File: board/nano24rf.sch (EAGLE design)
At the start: 26 parts, among them CN1 1X4-CLEANBIG, CN2 1X4-CLEANBIG, CN3 1X4-CLEANBIG, CN4 1X4-CLEANBIG

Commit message: before route
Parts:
- removed C1, C2: (no value), ATTAMI-V0.00:CAP0805
- removed CN1, CN2, CN3, CN4, I2CPORT: 1X4-CLEANBIG, adafruit:1X4-CLEANBIG
- removed FET1, FET2, JP6: (no value), ATTAMI-V0.00:HEADER-1X2ROUND
- removed SJ1, SJ2: JUMPER-PAD-3-2OF3_NC_BY_TRACE_SMALL, ATTAMI-V0.00:JUMPER-PAD-3-2OF3_NC_BY_TRACE_SMALL
- removed SW1: (no value), microbuilder:SWITCH_SPST
- removed U$2: NRF24, ATTAMI-V0.00:NRF24
- removed U2: (no value), microbuilder:VREG_SOT23SOT23_WIDE
- added D3, D4: (no value), dp_devices:DIODE-DO-214AC
- added Q3, Q4: (no value), adafruit:MOSFET-NWAVE
- added R5, R6: (no value), ATTAMI-V0.00:RESISTOR0805-RES
- added U$6, U$8: 1X3SMD, nanorf24:1X3SMD
- added U$7: 1X7-SMDPADS, nanorf24:1X7-SMDPADS
- JP3: device adafruit:PINHD-1X1CB -> pinhead+:PINHD-2X3SMT
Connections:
- removed net IRQ: U$2.IRQ
- removed net N$1 (its old number): D1.A, FET1.2, Q1.D
- removed net RAW: JP3.1, JP6.1, SW1.P
- removed net RX: CN4.3, JP2.14
- removed net TX: CN4.2, JP2.15
- removed net V-ADJ: C2.1, SJ1.1, U2.VOUT
- removed net V-NRF: SJ1.2, U$2.VCC
- new net D10: JP2.3, R3.1
- new net D9: JP2.4, R4.1
- new net FET01: D1.A, Q1.D, U$8.P$1
- new net FET02: D2.A, Q2.D, U$8.P$3
- new net FET03: D3.A, Q3.D, U$6.P$1
- new net FET04: D4.A, Q4.D, U$6.P$3
- new net N$5: Q4.G, R4.2
- net 3V3: no longer R3.2, R4.2, SJ1.3, SJ2.1
- net 5V: now also JP3.2, R5.1; no longer C1.1, CN4.1, JP1.12, SJ2.3, U2.VIN
- net CE: now also JP2.6, U$7.CE; no longer JP2.3, U$2.CE
- net CSN: now also JP2.5, U$7.CSN; no longer JP2.4, U$2.CSN
- net D3: no longer R1.1
- net D6: now also R1.1
- net GND: now also JP3.6, Q3.S, Q4.S, R6.1, U$7.GND; no longer C1.2, C2.2, CN4.4, I2CPORT.4, JP6.2, U$2.GND, U2.GND
- net MISO: now also JP3.1, U$7.MISO; no longer JP2.1, U$2.MISO
- net MOSI: now also JP3.4, U$7.MOSI; no longer JP2.2, U$2.MOSI
- net N$4: now also Q3.G, R3.2; no longer D2.A, FET2.2, Q2.D
- net N$6: now also R5.2, R6.2, U$7.3V3; no longer I2CPORT.3, SJ2.2
- net RST: now also JP3.5; no longer JP2.13
- net SCK: now also JP3.3, U$7.SCK; no longer JP1.1, U$2.SCK
- net SCL: no longer I2CPORT.1, R4.1
- net SDA: no longer I2CPORT.2, R3.1
- net VIN: now also D3.C, D4.C, U$6.P$2, U$8.P$2; no longer FET1.1, FET2.1, SW1.S
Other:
- note added: "mosfets"
- note removed: "* 5V on the right rail should not be connected to nano! this location is originaly for a reset pin."
- note removed: "NRF24"
- moved on the sheet: D1, D2, Q1, Q2, R1, R2, R3, R4

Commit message: added lib, need to fix volt div placment
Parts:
- JP3: device pinhead+:PINHD-2X3SMT -> nano24rf:PINHD-2X3SMT
- U$7: device nanorf24:1X7-SMDPADS -> nano24rf:1X7-SMDPADS
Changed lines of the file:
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@@
 <part name="JP1" library="microbuilder" deviceset="HEADER-1X15" device=""/>
 <part name="JP2" library="microbuilder" deviceset="HEADER-1X15" device=""/>
-<part name="JP3" library="pinhead+" deviceset="PINHD-2X3" device="SMT"/>
-<part name="U$7" library="nanorf24" deviceset="1X7-SMDPADS" device=""/>
+<part name="JP3" library="nano24rf" deviceset="PINHD-2X3" device="SMT"/>
+<part name="U$7" library="nano24rf" deviceset="1X7-SMDPADS" device=""/>
 <part name="Q2" library="adafruit" deviceset="MOSFET-N" device="WAVE"/>
 <part name="D2" library="dp_devices" deviceset="DIODE" device="-DO-214AC"/>

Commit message: ready to grb
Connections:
- removed net N$1: Q2.G, R2.2
- removed net N$2: Q1.G, R1.2
- removed net N$4: Q3.G, R3.2
- removed net N$5: Q4.G, R4.2
- net 5V: now also R1.1; no longer R5.1
- net D10: now also Q3.G, R5.2; no longer R3.1
- net D5: now also Q2.G, R4.2; no longer R2.1
- net D6: now also Q1.G, R3.2; no longer R1.1
- net D9: now also Q4.G, R6.2; no longer R4.1
- net GND: now also R2.1, R3.1, R4.1, R5.1
- net N$6: now also R1.2, R2.2; no longer R5.2, R6.2
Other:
- moved on the sheet: R1, R2, R3, R4, R5, R6
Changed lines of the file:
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@@
 <part name="D1" library="dp_devices" deviceset="DIODE" device="-DO-214AC"/>
 <part name="U$3" library="ATTAMI-V0.00" deviceset="GND" device=""/>
-<part name="R1" library="ATTAMI-V0.00" deviceset="RESISTOR" device="0805-RES"/>
 <part name="U$5" library="ATTAMI-V0.00" deviceset="GND" device=""/>
 <part name="JP1" library="microbuilder" deviceset="HEADER-1X15" device=""/>
@@
 <part name="D2" library="dp_devices" deviceset="DIODE" device="-DO-214AC"/>
 <part name="U$1" library="ATTAMI-V0.00" deviceset="GND" device=""/>
-<part name="R2" library="ATTAMI-V0.00" deviceset="RESISTOR" device="0805-RES"/>
 <part name="Q3" library="adafruit" deviceset="MOSFET-N" device="WAVE"/>
 <part name="D3" library="dp_devices" deviceset="DIODE" device="-DO-214AC"/>
 <part name="U$2" library="ATTAMI-V0.00" deviceset="GND" device=""/>
-<part name="R3" library="ATTAMI-V0.00" deviceset="RESISTOR" device="0805-RES"/>
 <part name="Q4" library="adafruit" deviceset="MOSFET-N" device="WAVE"/>
 <part name="D4" library="dp_devices" deviceset="DIODE" device="-DO-214AC"/>
 <part name="U$4" library="ATTAMI-V0.00" deviceset="GND" device=""/>
-<part name="R4" library="ATTAMI-V0.00" deviceset="RESISTOR" device="0805-RES"/>
 <part name="U$6" library="nanorf24" deviceset="1X3SMD" device=""/>
 <part name="U$8" library="nanorf24" deviceset="1X3SMD" device=""/>
+<part name="R1" library="ATTAMI-V0.00" deviceset="RESISTOR" device="0805-RES"/>
+<part name="R2" library="ATTAMI-V0.00" deviceset="RESISTOR" device="0805-RES"/>
+<part name="R4" library="ATTAMI-V0.00" deviceset="RESISTOR" device="0805-RES"/>
+<part name="R3" library="ATTAMI-V0.00" deviceset="RESISTOR" device="0805-RES"/>
+<part name="R6" library="ATTAMI-V0.00" deviceset="RESISTOR" device="0805-RES"/>
 <part name="R5" library="ATTAMI-V0.00" deviceset="RESISTOR" device="0805-RES"/>
-<part name="R6" library="ATTAMI-V0.00" deviceset="RESISTOR" device="0805-RES"/>
 </parts>
 <sheets>
@@
 <instance part="D1" gate="D" x="35.56" y="104.14" rot="R180"/>
 <instance part="U$3" gate="1" x="38.1" y="86.36"/>
-<instance part="R1" gate="G$1" x="25.4" y="93.98"/>
 <instance part="U$5" gate="1" x="27.94" y="27.94"/>
 <instance part="JP1" gate="G$1" x="45.72" y="48.26"/>
@@
 <instance part="D2" gate="D" x="35.56" y="132.08" rot="R180"/>
 <instance part="U$1" gate="1" x="38.1" y="114.3"/>
-<instance part="R2" gate="G$1" x="25.4" y="121.92"/>
 <instance part="Q3" gate="G$1" x="106.68" y="93.98"/>
 <instance part="D3" gate="D" x="106.68" y="101.6" rot="R180"/>
 <instance part="U$2" gate="1" x="109.22" y="83.82"/>
-<instance part="R3" gate="G$1" x="96.52" y="91.44"/>
 <instance part="Q4" gate="G$1" x="106.68" y="121.92"/>
 <instance part="D4" gate="D" x="106.68" y="129.54" rot="R180"/>
 <instance part="U$4" gate="1" x="109.22" y="111.76"/>
-<instance part="R4" gate="G$1" x="96.52" y="119.38"/>
 <instance part="U$6" gate="G$1" x="147.32" y="104.14" rot="R90"/>
 <instance part="U$8" gate="G$1" x="76.2" y="106.68" rot="R90"/>
-<instance part="R5" gate="G$1" x="73.66" y="15.24"/>
-<instance part="R6" gate="G$1" x="73.66" y="10.16"/>
+<instance part="R1" gate="G$1" x="73.66" y="15.24"/>
+<instance part="R2" gate="G$1" x="73.66" y="10.16"/>
+<instance part="R4" gate="G$1" x="30.48" y="116.84" rot="R90"/>
+<instance part="R3" gate="G$1" x="30.48" y="88.9" rot="R90"/>
+<instance part="R6" gate="G$1" x="101.6" y="114.3" rot="R90"/>
+<instance part="R5" gate="G$1" x="101.6" y="86.36" rot="R90"/>
 </instances>
 <busses>
@@
 <pinref part="U$3" gate="1" pin="GND"/>
 <wire x1="38.1" y1="88.9" x2="38.1" y2="91.44" width="0.1524" layer="91"/>
+<pinref part="R3" gate="G$1" pin="1"/>
+<wire x1="30.48" y1="83.82" x2="33.02" y2="83.82" width="0.1524" layer="91"/>
+<wire x1="33.02" y1="83.82" x2="33.02" y2="88.9" width="0.1524" layer="91"/>
+<wire x1="33.02" y1="88.9" x2="38.1" y2="88.9" width="0.1524" layer="91"/>
+<junction x="38.1" y="88.9"/>
 </segment>
 <segment>
@@
 <wire x1="58.42" y1="10.16" x2="68.58" y2="10.16" width="0.1524" layer="91"/>
 <label x="63.5" y="10.16" size="1.778" layer="95"/>
-<pinref part="R6" gate="G$1" pin="1"/>
+<pinref part="R2" gate="G$1" pin="1"/>
 </segment>
 <segment>
@@
 <pinref part="U$1" gate="1" pin="GND"/>
 <wire x1="38.1" y1="116.84" x2="38.1" y2="119.38" width="0.1524" layer="91"/>
+<pinref part="R4" gate="G$1" pin="1"/>
+<wire x1="30.48" y1="111.76" x2="33.02" y2="111.76" width="0.1524" layer="91"/>
+<wire x1="33.02" y1="111.76" x2="33.02" y2="116.84" width="0.1524" layer="91"/>
+<wire x1="33.02" y1="116.84" x2="38.1" y2="116.84" width="0.1524" layer="91"/>
+<junction x="38.1" y="116.84"/>
 </segment>
 <segment>
@@
 <pinref part="U$2" gate="1" pin="GND"/>
 <wire x1="109.22" y1="86.36" x2="109.22" y2="88.9" width="0.1524" layer="91"/>
+<pinref part="R5" gate="G$1" pin="1"/>
+<wire x1="101.6" y1="81.28" x2="104.14" y2="81.28" width="0.1524" layer="91"/>
+<wire x1="104.14" y1="81.28" x2="104.14" y2="86.36" width="0.1524" layer="91"/>
+<wire x1="104.14" y1="86.36" x2="109.22" y2="86.36" width="0.1524" layer="91"/>
+<junction x="109.22" y="86.36"/>
 </segment>
 <segment>
@@
 <pinref part="U$4" gate="1" pin="GND"/>
 <wire x1="109.22" y1="114.3" x2="109.22" y2="116.84" width="0.1524" layer="91"/>
+<pinref part="R6" gate="G$1" pin="1"/>
+<wire x1="101.6" y1="109.22" x2="104.14" y2="109.22" width="0.1524" layer="91"/>
+<wire x1="104.14" y1="109.22" x2="104.14" y2="114.3" width="0.1524" layer="91"/>
+<wire x1="104.14" y1="114.3" x2="109.22" y2="114.3" width="0.1524" layer="91"/>
+<junction x="109.22" y="114.3"/>
 </segment>
 </net>
@@
 </segment>
 </net>
-<net name="N$2" class="0">
-<segment>
-<pinref part="Q1" gate="G$1" pin="G"/>
-<pinref part="R1" gate="G$1" pin="2"/>
-<wire x1="30.48" y1="93.98" x2="33.02" y2="93.98" width="0.1524" layer="91"/>
-</segment>
-</net>
 <net name="D5" class="0">
 <segment>
@@
 </segment>
 <segment>
-<pinref part="R2" gate="G$1" pin="1"/>
-<wire x1="20.32" y1="121.92" x2="12.7" y2="121.92" width="0.1524" layer="91"/>
 <label x="15.24" y="121.92" size="1.778" layer="95"/>
+<pinref part="Q2" gate="G$1" pin="G"/>
+<wire x1="30.48" y1="121.92" x2="33.02" y2="121.92" width="0.1524" layer="91"/>
+<pinref part="R4" gate="G$1" pin="2"/>
+<wire x1="12.7" y1="121.92" x2="30.48" y2="121.92" width="0.1524" layer="91"/>
+<junction x="30.48" y="121.92"/>
 </segment>
 </net>
@@
 </segment>
 <segment>
-<pinref part="R1" gate="G$1" pin="1"/>
-<wire x1="20.32" y1="93.98" x2="12.7" y2="93.98" width="0.1524" layer="91"/>
 <label x="15.24" y="93.98" size="1.778" layer="95"/>
+<pinref part="Q1" gate="G$1" pin="G"/>
+<wire x1="30.48" y1="93.98" x2="33.02" y2="93.98" width="0.1524" layer="91"/>
+<pinref part="R3" gate="G$1" pin="2"/>
+<wire x1="12.7" y1="93.98" x2="30.48" y2="93.98" width="0.1524" layer="91"/>
+<junction x="30.48" y="93.98"/>
 </segment>
 </net>
@@
 <wire x1="58.42" y1="15.24" x2="68.58" y2="15.24" width="0.1524" layer="91"/>
 <label x="63.5" y="15.24" size="1.778" layer="95"/>
-<pinref part="R5" gate="G$1" pin="1"/>
+<pinref part="R1" gate="G$1" pin="1"/>
 </segment>
 </net>
@@
 </segment>
 <segment>
-<pinref part="R3" gate="G$1" pin="1"/>
-<wire x1="91.44" y1="91.44" x2="83.82" y2="91.44" width="0.1524" layer="91"/>
 <label x="86.36" y="91.44" size="1.778" layer="95"/>
+<pinref part="Q3" gate="G$1" pin="G"/>
+<wire x1="101.6" y1="91.44" x2="104.14" y2="91.44" width="0.1524" layer="91"/>
+<pinref part="R5" gate="G$1" pin="2"/>
+<wire x1="83.82" y1="91.44" x2="101.6" y2="91.44" width="0.1524" layer="91"/>
+<junction x="101.6" y="91.44"/>
 </segment>
 </net>
@@
 </segment>
 <segment>
-<pinref part="R4" gate="G$1" pin="1"/>
-<wire x1="91.44" y1="119.38" x2="83.82" y2="119.38" width="0.1524" layer="91"/>
 <label x="86.36" y="119.38" size="1.778" layer="95"/>
+<pinref part="Q4" gate="G$1" pin="G"/>
+<wire x1="101.6" y1="119.38" x2="104.14" y2="119.38" width="0.1524" layer="91"/>
+<pinref part="R6" gate="G$1" pin="2"/>
+<wire x1="101.6" y1="119.38" x2="83.82" y2="119.38" width="0.1524" layer="91"/>
+<junction x="101.6" y="119.38"/>
 </segment>
 </net>
@@
 </segment>
 </net>
-<net name="N$1" class="0">
-<segment>
-<pinref part="Q2" gate="G$1" pin="G"/>
-<pinref part="R2" gate="G$1" pin="2"/>
-<wire x1="30.48" y1="121.92" x2="33.02" y2="121.92" width="0.1524" layer="91"/>
-</segment>
-</net>
 <net name="FET03" class="0">
 <segment>
@@
 </segment>
 </net>
-<net name="N$4" class="0">
-<segment>
-<pinref part="Q3" gate="G$1" pin="G"/>
-<pinref part="R3" gate="G$1" pin="2"/>
-<wire x1="101.6" y1="91.44" x2="104.14" y2="91.44" width="0.1524" layer="91"/>
-</segment>
-</net>
 <net name="FET04" class="0">
 <segment>
@@
 </segment>
 </net>
-<net name="N$5" class="0">
-<segment>
-<pinref part="Q4" gate="G$1" pin="G"/>
-<pinref part="R4" gate="G$1" pin="2"/>
-<wire x1="101.6" y1="119.38" x2="104.14" y2="119.38" width="0.1524" layer="91"/>
-</segment>
-</net>
 <net name="N$6" class="0">
 <segment>
 <wire x1="81.28" y1="2.54" x2="81.28" y2="10.16" width="0.1524" layer="91"/>
-<pinref part="R5" gate="G$1" pin="2"/>
+<pinref part="R1" gate="G$1" pin="2"/>
 <wire x1="81.28" y1="10.16" x2="81.28" y2="15.24" width="0.1524" layer="91"/>
 <wire x1="81.28" y1="15.24" x2="78.74" y2="15.24" width="0.1524" layer="91"/>
 <pinref part="U$7" gate="G$1" pin="3V3"/>
-<pinref part="R6" gate="G$1" pin="2"/>
+<pinref part="R2" gate="G$1" pin="2"/>
 <wire x1="78.74" y1="10.16" x2="81.28" y2="10.16" width="0.1524" layer="91"/>
 <junction x="81.28" y="10.16"/>

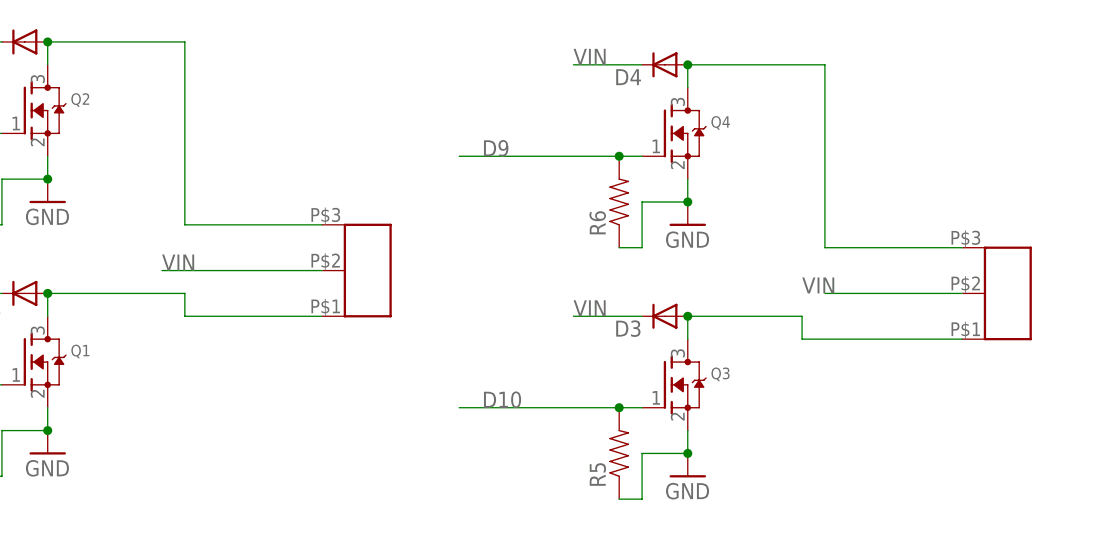
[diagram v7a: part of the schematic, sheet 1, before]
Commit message: added FATPAD4
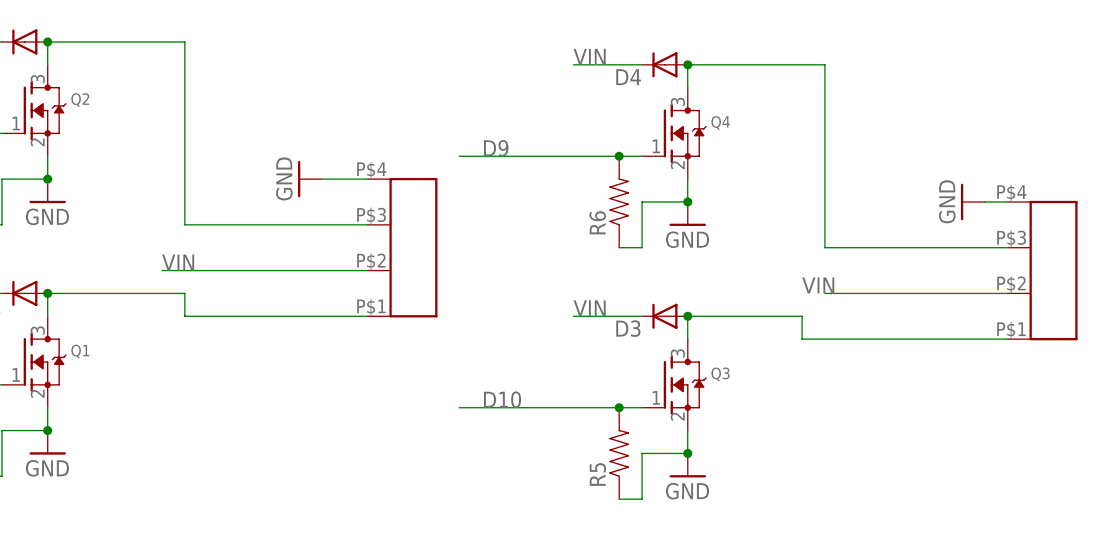
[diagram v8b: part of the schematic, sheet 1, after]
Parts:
- U$6, U$8: value 1X3SMD -> FATPAD4; device nanorf24:1X3SMD -> nano24rf:FATPAD4
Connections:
- net GND: now also U$6.P$4, U$8.P$4
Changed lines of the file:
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@@
 <part name="D4" library="dp_devices" deviceset="DIODE" device="-DO-214AC"/>
 <part name="U$4" library="ATTAMI-V0.00" deviceset="GND" device=""/>
-<part name="U$6" library="nanorf24" deviceset="1X3SMD" device=""/>
-<part name="U$8" library="nanorf24" deviceset="1X3SMD" device=""/>
+<part name="U$6" library="nano24rf" deviceset="FATPAD4" device=""/>
+<part name="U$8" library="nano24rf" deviceset="FATPAD4" device=""/>
 <part name="R1" library="ATTAMI-V0.00" deviceset="RESISTOR" device="0805-RES"/>
 <part name="R2" library="ATTAMI-V0.00" deviceset="RESISTOR" device="0805-RES"/>
@@
 <part name="R6" library="ATTAMI-V0.00" deviceset="RESISTOR" device="0805-RES"/>
 <part name="R5" library="ATTAMI-V0.00" deviceset="RESISTOR" device="0805-RES"/>
+<part name="U$9" library="ATTAMI-V0.00" deviceset="GND" device=""/>
+<part name="U$10" library="ATTAMI-V0.00" deviceset="GND" device=""/>
 </parts>
 <sheets>
@@
 <instance part="R6" gate="G$1" x="101.6" y="114.3" rot="R90"/>
 <instance part="R5" gate="G$1" x="101.6" y="86.36" rot="R90"/>
+<instance part="U$9" gate="1" x="139.7" y="114.3" rot="R270"/>
+<instance part="U$10" gate="1" x="66.04" y="116.84" rot="R270"/>
 </instances>
 <busses>
@@
 <junction x="109.22" y="114.3"/>
 </segment>
+<segment>
+<pinref part="U$10" gate="1" pin="GND"/>
+<pinref part="U$8" gate="G$1" pin="P$4"/>
+<wire x1="68.58" y1="116.84" x2="73.66" y2="116.84" width="0.1524" layer="91"/>
+</segment>
+<segment>
+<pinref part="U$6" gate="G$1" pin="P$4"/>
+<pinref part="U$9" gate="1" pin="GND"/>
+<wire x1="144.78" y1="114.3" x2="142.24" y2="114.3" width="0.1524" layer="91"/>
+</segment>
 </net>
 <net name="FET01" class="0">
@@
 <wire x1="38.1" y1="101.6" x2="38.1" y2="104.14" width="0.1524" layer="91"/>
 <junction x="38.1" y="104.14"/>
-<wire x1="68.58" y1="101.6" x2="53.34" y2="101.6" width="0.1524" layer="91"/>
+<wire x1="73.66" y1="101.6" x2="53.34" y2="101.6" width="0.1524" layer="91"/>
 <wire x1="53.34" y1="101.6" x2="53.34" y2="104.14" width="0.1524" layer="91"/>
 <wire x1="53.34" y1="104.14" x2="38.1" y2="104.14" width="0.1524" layer="91"/>
@@
 </segment>
 <segment>
-<wire x1="68.58" y1="106.68" x2="50.8" y2="106.68" width="0.1524" layer="91"/>
+<wire x1="73.66" y1="106.68" x2="50.8" y2="106.68" width="0.1524" layer="91"/>
 <label x="50.8" y="106.68" size="1.778" layer="95"/>
 <pinref part="U$8" gate="G$1" pin="P$2"/>
@@
 </segment>
 <segment>
-<wire x1="139.7" y1="104.14" x2="124.46" y2="104.14" width="0.1524" layer="91"/>
+<wire x1="144.78" y1="104.14" x2="124.46" y2="104.14" width="0.1524" layer="91"/>
 <label x="121.92" y="104.14" size="1.778" layer="95"/>
 <pinref part="U$6" gate="G$1" pin="P$2"/>
@@
 <junction x="38.1" y="132.08"/>
 <wire x1="53.34" y1="132.08" x2="38.1" y2="132.08" width="0.1524" layer="91"/>
-<wire x1="68.58" y1="111.76" x2="53.34" y2="111.76" width="0.1524" layer="91"/>
+<wire x1="73.66" y1="111.76" x2="53.34" y2="111.76" width="0.1524" layer="91"/>
 <wire x1="53.34" y1="111.76" x2="53.34" y2="132.08" width="0.1524" layer="91"/>
 <pinref part="U$8" gate="G$1" pin="P$3"/>
@@
 <wire x1="109.22" y1="99.06" x2="109.22" y2="101.6" width="0.1524" layer="91"/>
 <junction x="109.22" y="101.6"/>
-<wire x1="139.7" y1="99.06" x2="121.92" y2="99.06" width="0.1524" layer="91"/>
+<wire x1="144.78" y1="99.06" x2="121.92" y2="99.06" width="0.1524" layer="91"/>
 <wire x1="121.92" y1="99.06" x2="121.92" y2="101.6" width="0.1524" layer="91"/>
 <wire x1="121.92" y1="101.6" x2="109.22" y2="101.6" width="0.1524" layer="91"/>
@@
 <junction x="109.22" y="129.54"/>
 <wire x1="124.46" y1="129.54" x2="109.22" y2="129.54" width="0.1524" layer="91"/>
-<wire x1="139.7" y1="109.22" x2="124.46" y2="109.22" width="0.1524" layer="91"/>
+<wire x1="144.78" y1="109.22" x2="124.46" y2="109.22" width="0.1524" layer="91"/>
 <wire x1="124.46" y1="109.22" x2="124.46" y2="129.54" width="0.1524" layer="91"/>
 <pinref part="U$6" gate="G$1" pin="P$3"/>
